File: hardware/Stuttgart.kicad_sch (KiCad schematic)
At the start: 4 parts

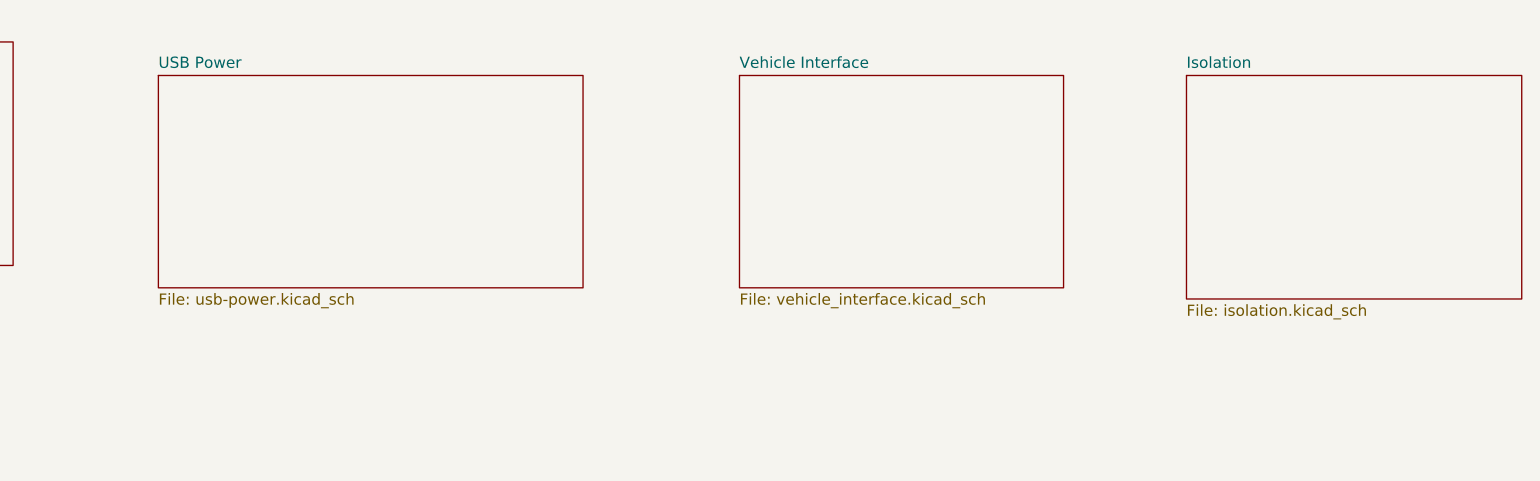
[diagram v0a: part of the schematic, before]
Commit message: Moved GND points, revised DCDC and base USB Work
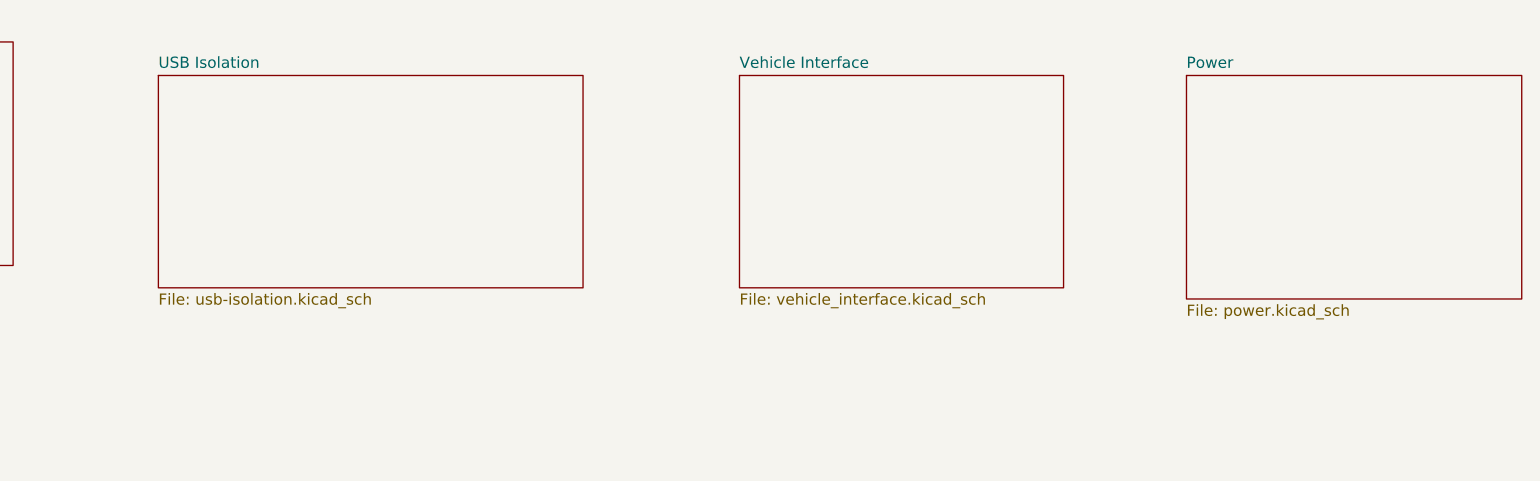
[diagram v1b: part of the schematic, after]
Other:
- sheet Isolation renamed Power
- sheet USB Power renamed USB Isolation
- sheet Power: file isolation.kicad_sch -> power.kicad_sch
- sheet USB Isolation: file usb-power.kicad_sch -> usb-isolation.kicad_sch
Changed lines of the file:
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@@
 			(color 0 0 0 0)
 		)
-		(property "Sheetname" "USB Power"
+		(property "Sheetname" "USB Isolation"
 			(at 82.55 34.8484 0)
 			(show_name no)
@@
 			)
 		)
-		(property "Sheetfile" "usb-power.kicad_sch"
+		(property "Sheetfile" "usb-isolation.kicad_sch"
 			(at 82.55 60.2746 0)
 			(show_name no)
@@
 			(color 0 0 0 0)
 		)
-		(property "Sheetname" "Isolation"
+		(property "Sheetname" "Power"
 			(at 199.39 34.8484 0)
 			(show_name no)
@@
 			)
 		)
-		(property "Sheetfile" "isolation.kicad_sch"
+		(property "Sheetfile" "power.kicad_sch"
 			(at 199.39 61.5446 0)
 			(show_name no)

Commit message: Board outline and fiducials
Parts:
- added FID1, FID2, FID3, FID4, FID5: Fiducial, Fiducial:Fiducial_1mm_Mask2mm, symbol Mechanical:Fiducial
